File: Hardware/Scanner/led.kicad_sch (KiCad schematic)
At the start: 20 parts, among them U5 TLC59208FIPWR

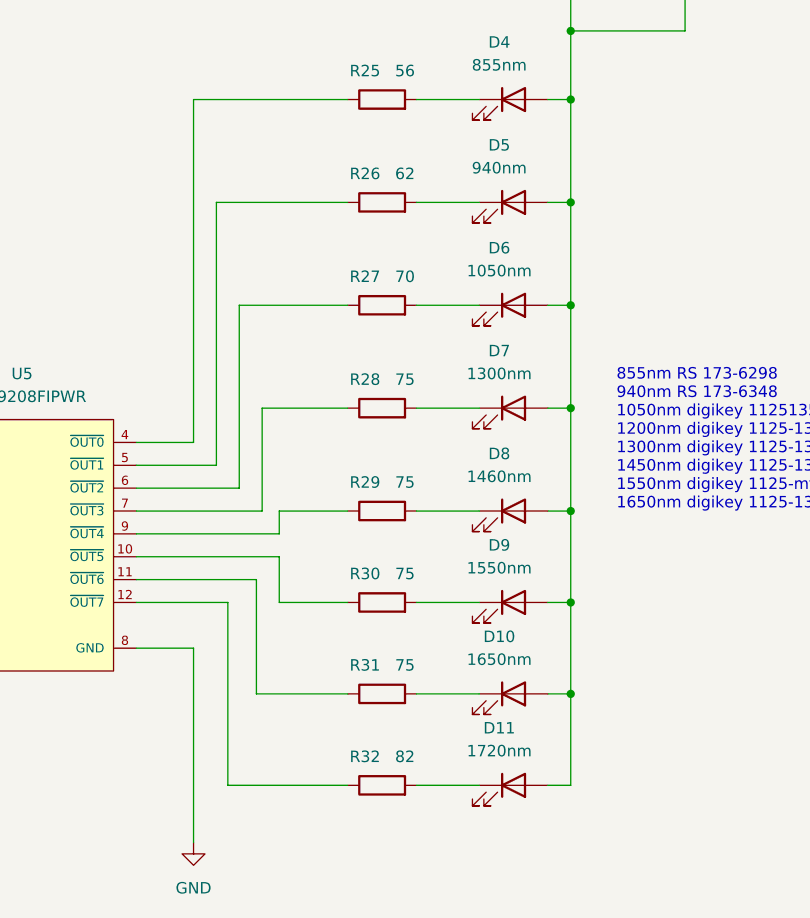
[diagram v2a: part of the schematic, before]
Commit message: LED ressistor changes
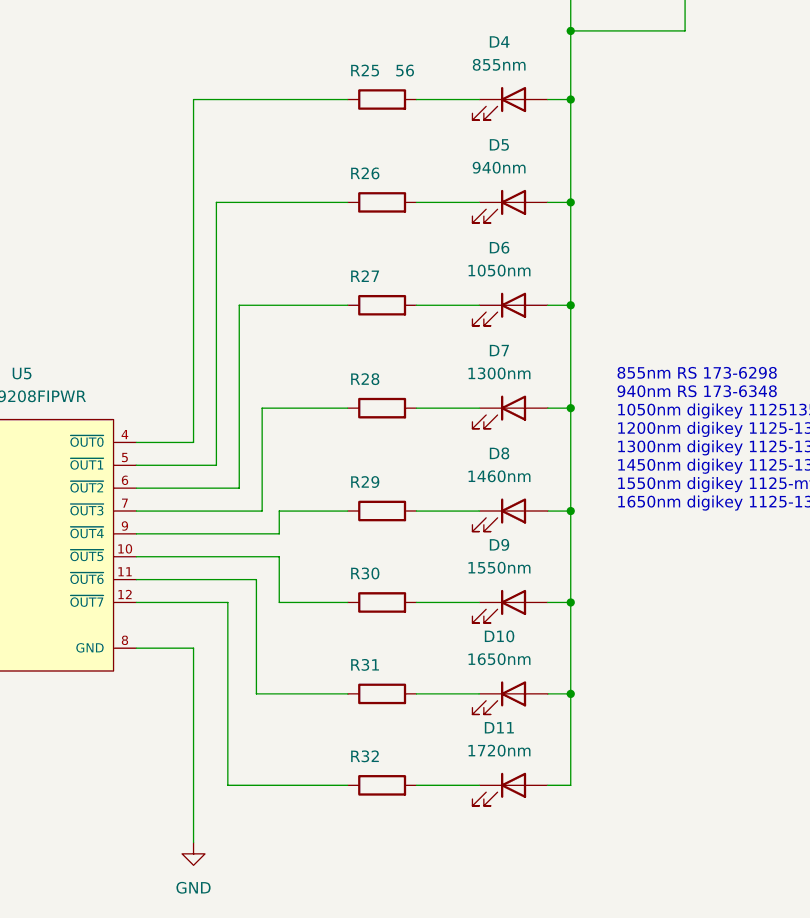
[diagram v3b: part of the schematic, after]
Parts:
- R26: value 62 -> (none)
- R27: value 70 -> (none)
- R28, R29, R30: value 75 -> (none)
- R31: value 75 -> (none); footprint Resistor_SMD:R_0603_1608Metric_Pad0.98x0.95mm_HandSolder -> (none)
- R32: value 82 -> (none)
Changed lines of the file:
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@@
     (in_bom yes) (on_board yes)
     (property "Reference" "R32" (id 0) (at 185.42 127.635 90))
-    (property "Value" "82" (id 1) (at 189.865 127.635 90))
+    (property "Value" "" (id 1) (at 189.865 127.635 90))
     (property "Footprint" "Resistor_SMD:R_0603_1608Metric_Pad0.98x0.95mm_HandSolder" (id 2) (at 187.325 132.588 90)
       (effects (font (size 1.27 1.27)) hide)
@@
     (in_bom yes) (on_board yes)
     (property "Reference" "R26" (id 0) (at 185.42 62.865 90))
-    (property "Value" "62" (id 1) (at 189.865 62.865 90))
+    (property "Value" "" (id 1) (at 189.865 62.865 90))
     (property "Footprint" "Resistor_SMD:R_0603_1608Metric_Pad0.98x0.95mm_HandSolder" (id 2) (at 187.325 67.818 90)
       (effects (font (size 1.27 1.27)) hide)
@@
     (in_bom yes) (on_board yes)
     (property "Reference" "R30" (id 0) (at 185.42 107.315 90))
-    (property "Value" "75" (id 1) (at 189.865 107.315 90))
+    (property "Value" "" (id 1) (at 189.865 107.315 90))
     (property "Footprint" "Resistor_SMD:R_0603_1608Metric_Pad0.98x0.95mm_HandSolder" (id 2) (at 187.325 112.268 90)
       (effects (font (size 1.27 1.27)) hide)
@@
     (in_bom yes) (on_board yes)
     (property "Reference" "R29" (id 0) (at 185.42 97.155 90))
-    (property "Value" "75" (id 1) (at 189.865 97.155 90))
+    (property "Value" "" (id 1) (at 189.865 97.155 90))
     (property "Footprint" "Resistor_SMD:R_0603_1608Metric_Pad0.98x0.95mm_HandSolder" (id 2) (at 187.325 102.108 90)
       (effects (font (size 1.27 1.27)) hide)
@@
     (in_bom yes) (on_board yes)
     (property "Reference" "R31" (id 0) (at 185.42 117.475 90))
-    (property "Value" "75" (id 1) (at 189.865 117.475 90))
-    (property "Footprint" "Resistor_SMD:R_0603_1608Metric_Pad0.98x0.95mm_HandSolder" (id 2) (at 187.325 122.428 90)
+    (property "Value" "" (id 1) (at 189.865 117.475 90))
+    (property "Footprint" "" (id 2) (at 187.325 122.428 90)
       (effects (font (size 1.27 1.27)) hide)
     )
@@
     (in_bom yes) (on_board yes)
     (property "Reference" "R27" (id 0) (at 185.42 74.295 90))
-    (property "Value" "70" (id 1) (at 189.865 74.295 90))
+    (property "Value" "" (id 1) (at 189.865 74.295 90))
     (property "Footprint" "Resistor_SMD:R_0603_1608Metric_Pad0.98x0.95mm_HandSolder" (id 2) (at 187.325 79.248 90)
       (effects (font (size 1.27 1.27)) hide)
@@
     (in_bom yes) (on_board yes)
     (property "Reference" "R28" (id 0) (at 185.42 85.725 90))
-    (property "Value" "75" (id 1) (at 189.865 85.725 90))
+    (property "Value" "" (id 1) (at 189.865 85.725 90))
     (property "Footprint" "Resistor_SMD:R_0603_1608Metric_Pad0.98x0.95mm_HandSolder" (id 2) (at 187.325 90.678 90)
       (effects (font (size 1.27 1.27)) hide)

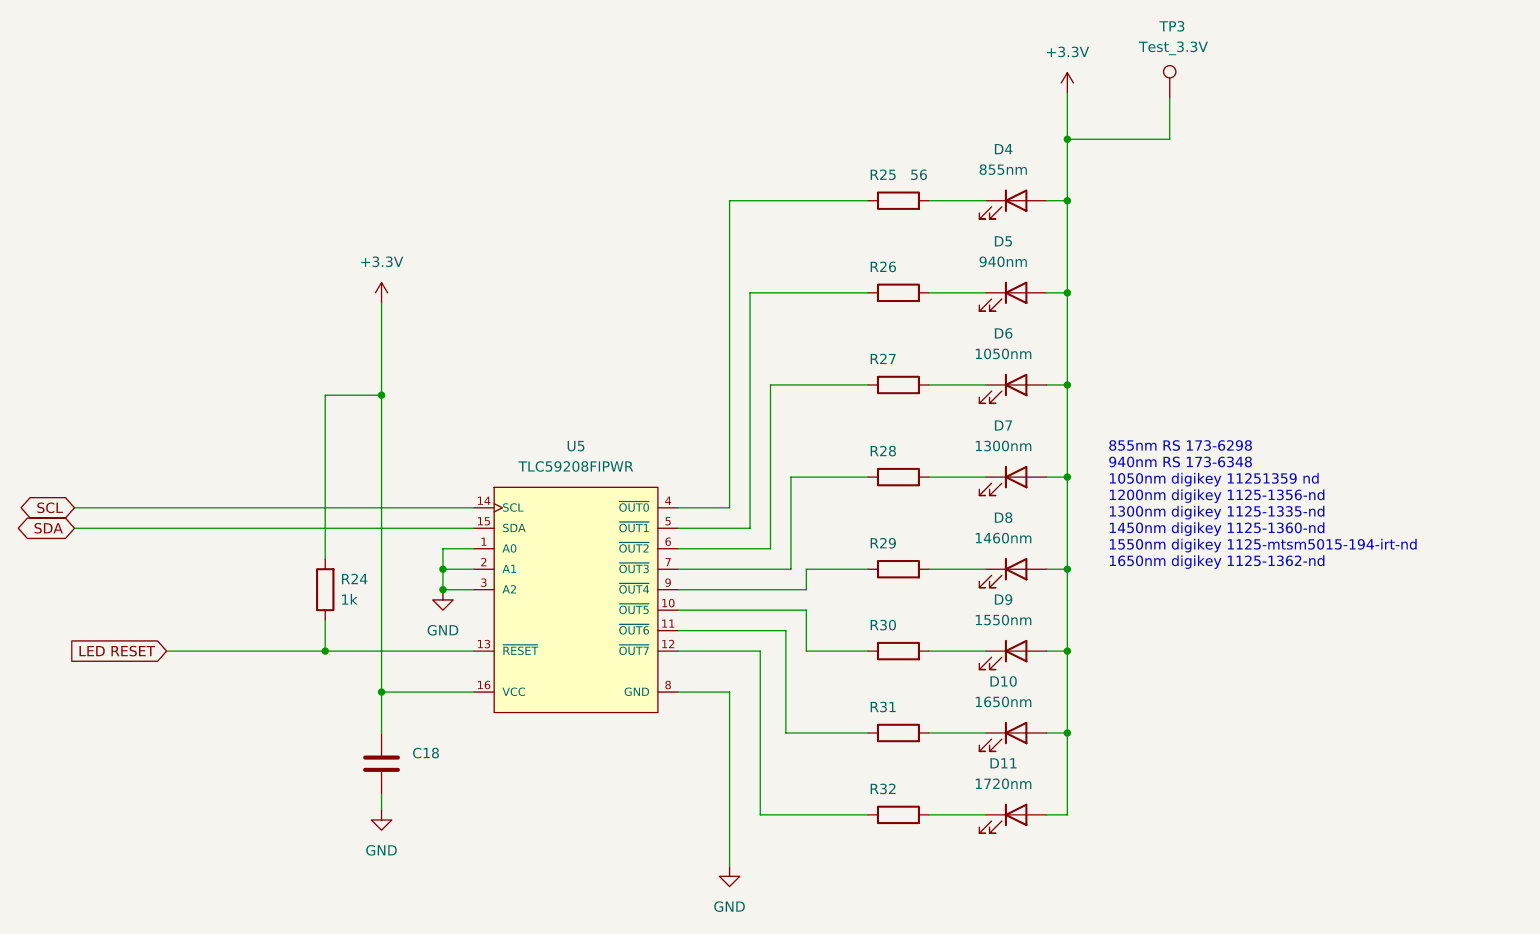
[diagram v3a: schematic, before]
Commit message: LAtching circuit for controller board + minors
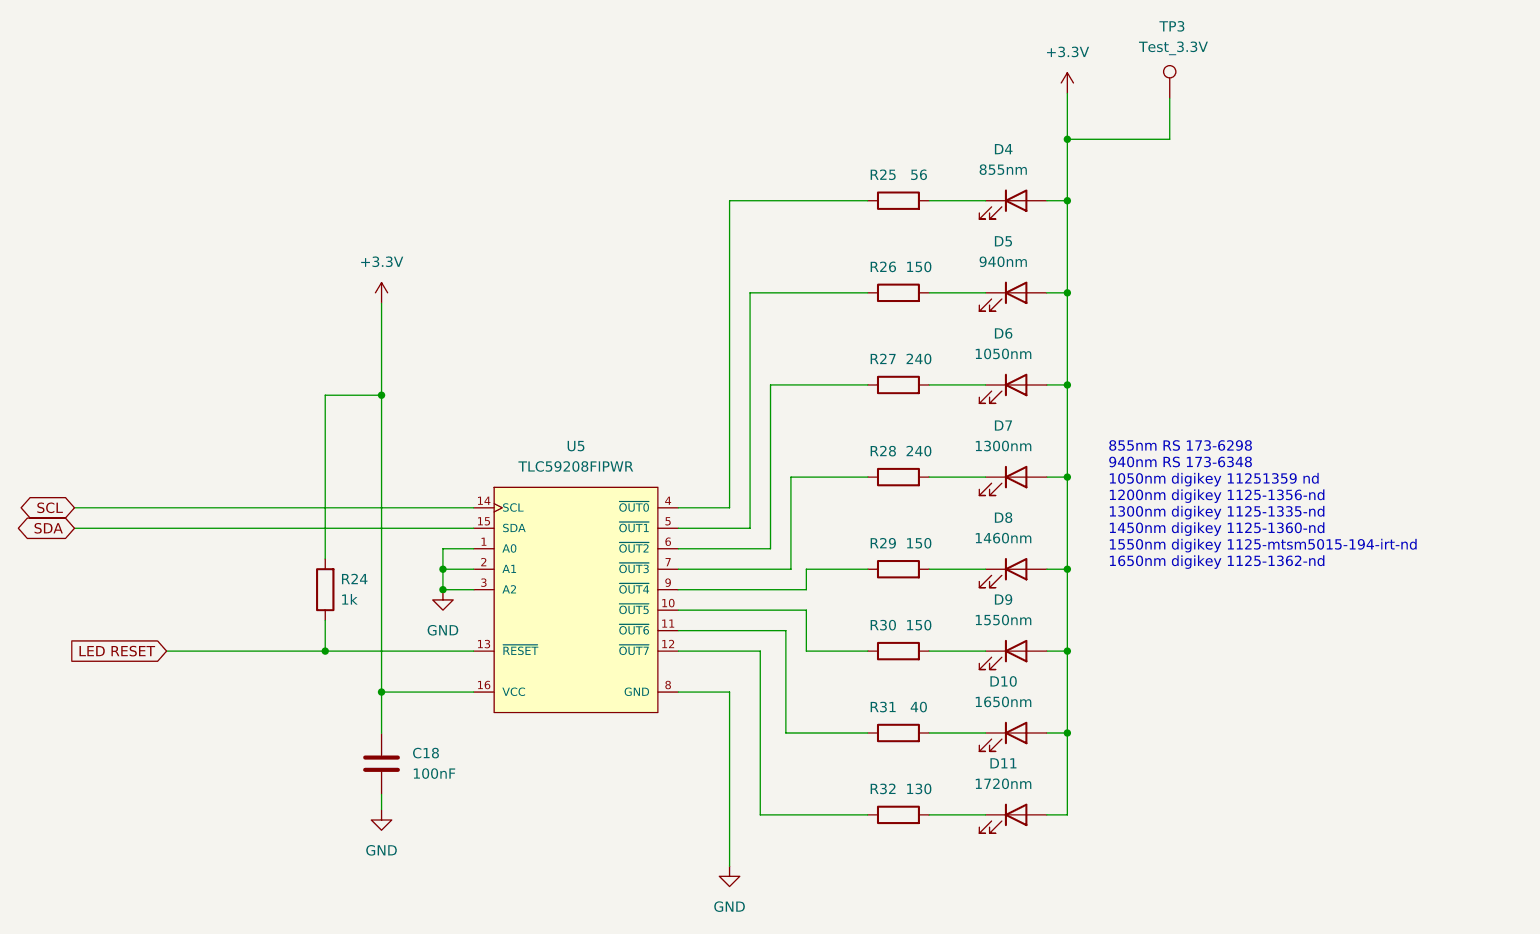
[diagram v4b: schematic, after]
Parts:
- C18: value (none) -> 100nF
- R26, R29, R30: value (none) -> 150
- R27, R28: value (none) -> 240
- R31: value (none) -> 40; footprint (none) -> Resistor_SMD:R_0603_1608Metric_Pad0.98x0.95mm_HandSolder
- R32: value (none) -> 130
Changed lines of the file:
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@@
     (in_bom yes) (on_board yes)
     (property "Reference" "R32" (id 0) (at 185.42 127.635 90))
-    (property "Value" "" (id 1) (at 189.865 127.635 90))
+    (property "Value" "130" (id 1) (at 189.865 127.635 90))
     (property "Footprint" "Resistor_SMD:R_0603_1608Metric_Pad0.98x0.95mm_HandSolder" (id 2) (at 187.325 132.588 90)
       (effects (font (size 1.27 1.27)) hide)
@@
     (in_bom yes) (on_board yes)
     (property "Reference" "R26" (id 0) (at 185.42 62.865 90))
-    (property "Value" "" (id 1) (at 189.865 62.865 90))
+    (property "Value" "150" (id 1) (at 189.865 62.865 90))
     (property "Footprint" "Resistor_SMD:R_0603_1608Metric_Pad0.98x0.95mm_HandSolder" (id 2) (at 187.325 67.818 90)
       (effects (font (size 1.27 1.27)) hide)
@@
       (effects (font (size 1.27 1.27)) (justify left))
     )
-    (property "Value" "" (id 1) (at 127 125.7299 0)
+    (property "Value" "100nF" (id 1) (at 127 125.7299 0)
       (effects (font (size 1.27 1.27)) (justify left))
     )
@@
     (in_bom yes) (on_board yes)
     (property "Reference" "R30" (id 0) (at 185.42 107.315 90))
-    (property "Value" "" (id 1) (at 189.865 107.315 90))
+    (property "Value" "150" (id 1) (at 189.865 107.315 90))
     (property "Footprint" "Resistor_SMD:R_0603_1608Metric_Pad0.98x0.95mm_HandSolder" (id 2) (at 187.325 112.268 90)
       (effects (font (size 1.27 1.27)) hide)
@@
     (in_bom yes) (on_board yes)
     (property "Reference" "R29" (id 0) (at 185.42 97.155 90))
-    (property "Value" "" (id 1) (at 189.865 97.155 90))
+    (property "Value" "150" (id 1) (at 189.865 97.155 90))
     (property "Footprint" "Resistor_SMD:R_0603_1608Metric_Pad0.98x0.95mm_HandSolder" (id 2) (at 187.325 102.108 90)
       (effects (font (size 1.27 1.27)) hide)
@@
     (in_bom yes) (on_board yes)
     (property "Reference" "R31" (id 0) (at 185.42 117.475 90))
-    (property "Value" "" (id 1) (at 189.865 117.475 90))
-    (property "Footprint" "" (id 2) (at 187.325 122.428 90)
+    (property "Value" "40" (id 1) (at 189.865 117.475 90))
+    (property "Footprint" "Resistor_SMD:R_0603_1608Metric_Pad0.98x0.95mm_HandSolder" (id 2) (at 187.325 122.428 90)
       (effects (font (size 1.27 1.27)) hide)
     )
@@
     (in_bom yes) (on_board yes)
     (property "Reference" "R27" (id 0) (at 185.42 74.295 90))
-    (property "Value" "" (id 1) (at 189.865 74.295 90))
+    (property "Value" "240" (id 1) (at 189.865 74.295 90))
     (property "Footprint" "Resistor_SMD:R_0603_1608Metric_Pad0.98x0.95mm_HandSolder" (id 2) (at 187.325 79.248 90)
       (effects (font (size 1.27 1.27)) hide)
@@
     (in_bom yes) (on_board yes)
     (property "Reference" "R28" (id 0) (at 185.42 85.725 90))
-    (property "Value" "" (id 1) (at 189.865 85.725 90))
+    (property "Value" "240" (id 1) (at 189.865 85.725 90))
     (property "Footprint" "Resistor_SMD:R_0603_1608Metric_Pad0.98x0.95mm_HandSolder" (id 2) (at 187.325 90.678 90)
       (effects (font (size 1.27 1.27)) hide)
